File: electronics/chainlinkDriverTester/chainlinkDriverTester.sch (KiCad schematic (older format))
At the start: 147 parts, among them J10 Sensor C, J11 Sensor D, J12 Motor E, J13 Motor F, J14 Sensor E, J15 Sensor F, J22 Power, J26 exp, J27 exp, J28 exp, J29 exp, J3 Motor A, J30 exp, J31 exp, J32 Conn_01x06_Female, J5 Motor B, J6 Motor C, J7 Motor D, J8 Sensor A, J9 Sensor B, U1 AP7361C-33E, U2 TTGO_TDisplay, U3 VN7007ALH, U4 MCP23017_SS, U5 INA219BxD, U6 SN74LV1T34DBV

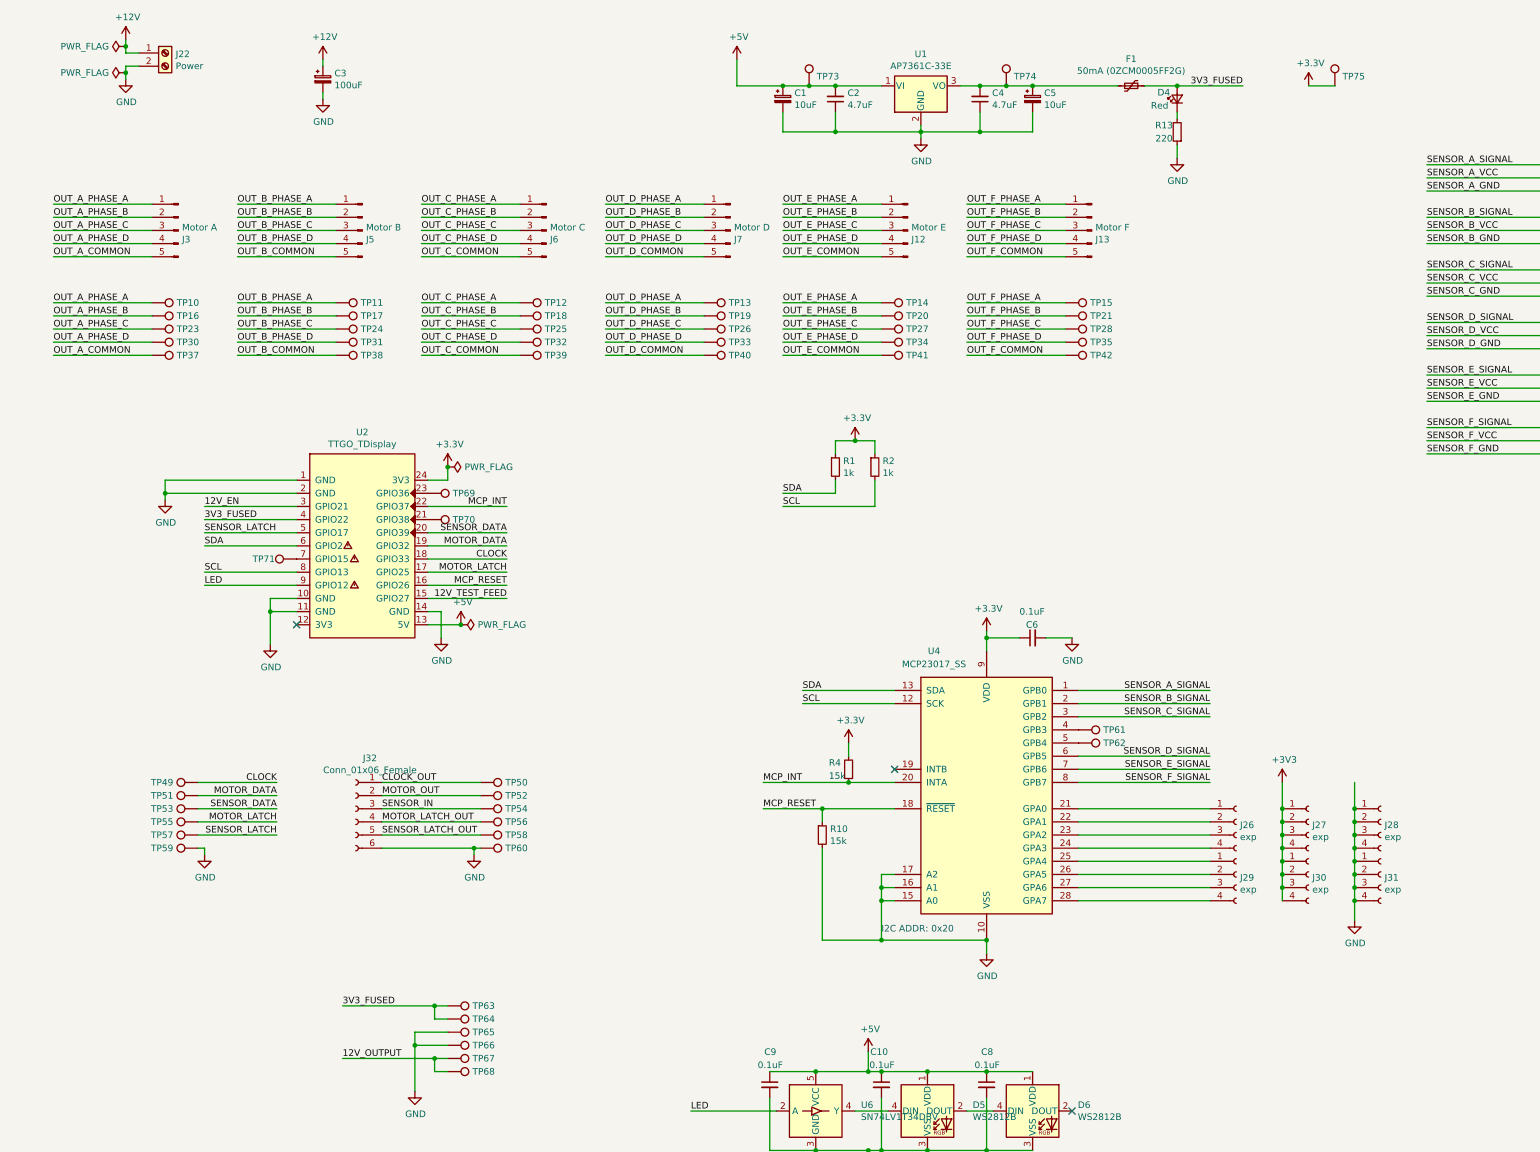
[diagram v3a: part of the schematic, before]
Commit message: PCB updates, add buzzer, add CI
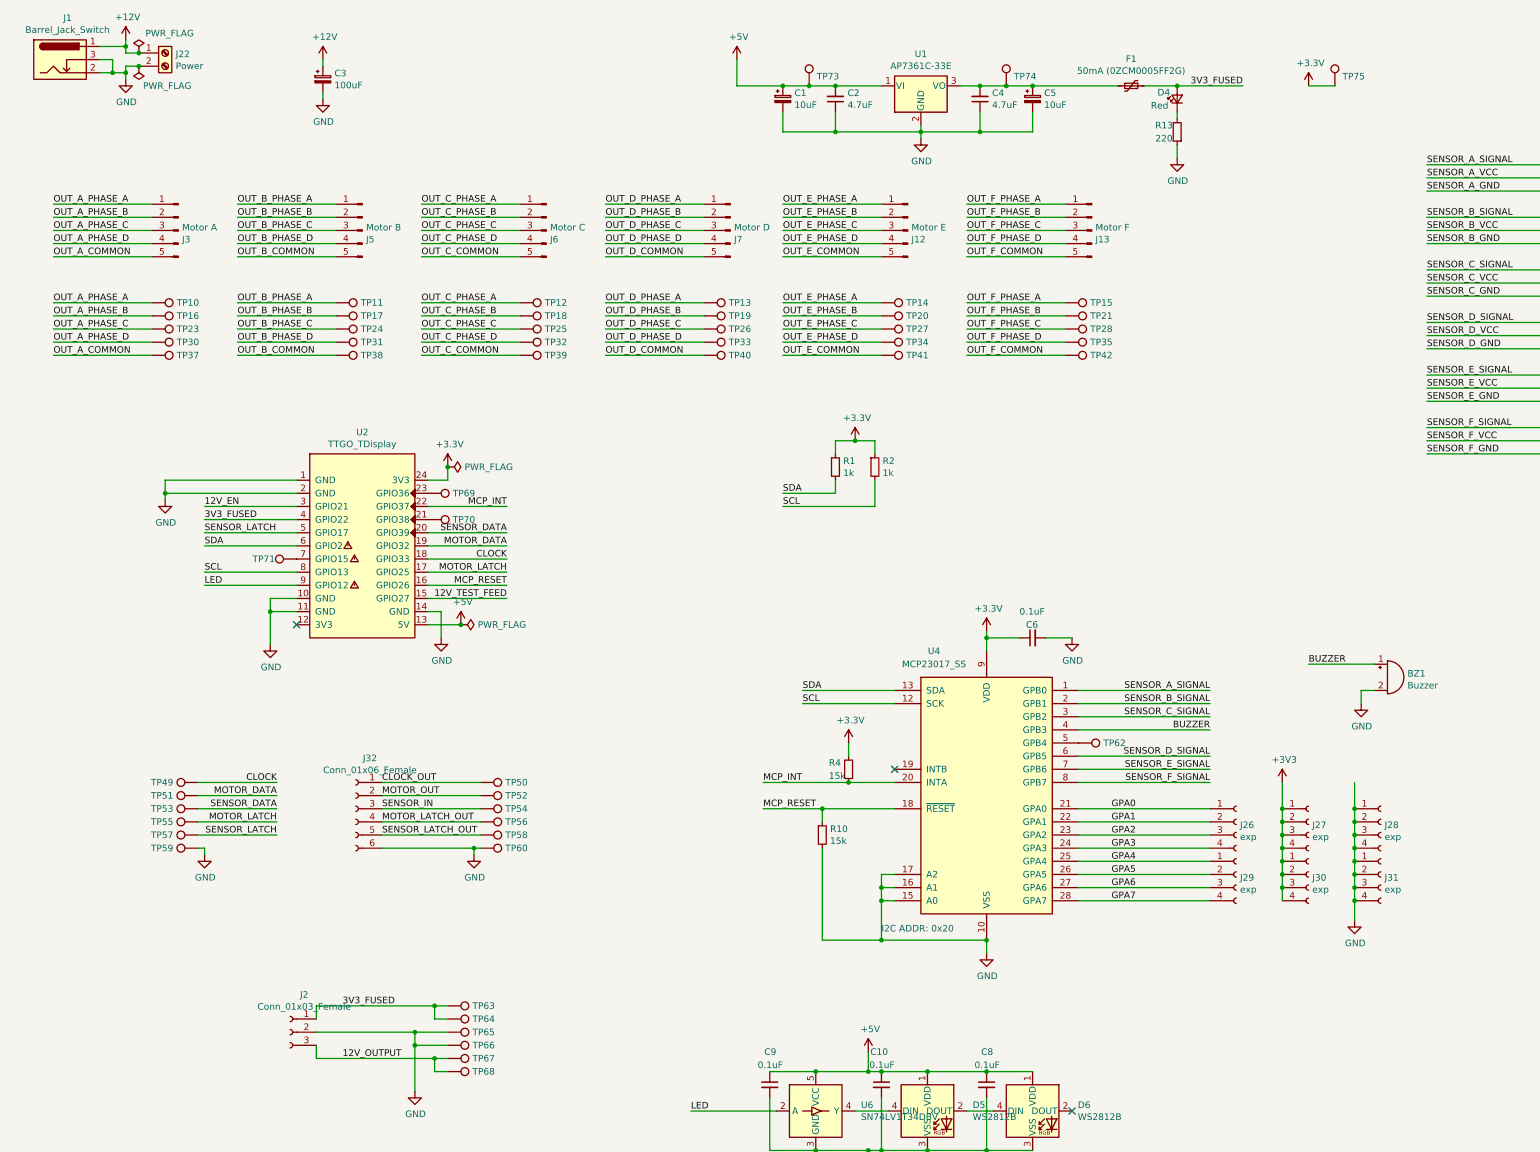
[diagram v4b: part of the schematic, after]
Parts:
- removed TP61: TestPoint, TestPoint:TestPoint_THTPad_D2.0mm_Drill1.0mm, symbol Connector:TestPoint
- added BZ1: Buzzer, Buzzer_Beeper:Buzzer_12x9.5RM7.6, symbol Device:Buzzer
- added J1: Barrel_Jack_Switch, PJ-202A:PJ-202A, symbol Connector:Barrel_Jack_Switch
- added J2: Conn_01x03_Female, Connector_PinSocket_2.54mm:PinSocket_1x03_P2.54mm_Vertical, symbol Connector:Conn_01x03_Female
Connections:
- net +12V: now also J1.1
- net 12V_OUTPUT: now also J2.3 (Pin_3)
- net 3V3_FUSED: now also J2.1 (Pin_1)
- net GND: now also BZ1.2 (+), J1.2, J1.3, J2.2 (Pin_2)
- net GPA0: now reaches J26.1 (Pin_1), U4.21 (GPA0)
- net GPA1: now reaches J26.2 (Pin_2), U4.22 (GPA1)
- net GPA2: now reaches J26.3 (Pin_3), U4.23 (GPA2)
- net GPA3: now reaches J26.4 (Pin_4), U4.24 (GPA3)
- net GPA4: now reaches J29.1 (Pin_1), U4.25 (GPA4)
- net GPA5: now reaches J29.2 (Pin_2), U4.26 (GPA5)
- net GPA6: now reaches J29.3 (Pin_3), U4.27 (GPA6)
- net GPA7: now reaches J29.4 (Pin_4), U4.28 (GPA7)
- net BUZZER: now reaches U4.4 (GPB3)
- net BUZZER: now also BZ1.1 (-)
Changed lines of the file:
@@
 Connection ~ 3650 8500
-Wire Wire Line
-	3650 8500 2950 8500
 Wire Wire Line
 	3750 8300 3500 8300
@@
 $EndComp
 Wire Wire Line
-	1300 1050 1300 1000
-Wire Wire Line
 	1300 950  1400 950
 Wire Wire Line
@@
 L power:PWR_FLAG #FLG0103
 U 1 1 6165DEB7
-P 1300 800
-F 0 "#FLG0103" H 1300 875 50  0001 C CNN
-F 1 "PWR_FLAG" V 1300 927 50  0000 L CNN
-F 2 "" H 1300 800 50  0001 C CNN
-F 3 "~" H 1300 800 50  0001 C CNN
-	1    1300 800
-	0    -1   -1   0
+P 1400 850
+F 0 "#FLG0103" H 1400 925 50  0001 C CNN
+F 1 "PWR_FLAG" H 1450 1000 50  0000 L CNN
+F 2 "" H 1400 850 50  0001 C CNN
+F 3 "~" H 1400 850 50  0001 C CNN
+	1    1400 850
+	1    0    0    -1
 $EndComp
 Connection ~ 1300 800
@@
 Text Label 2950 8100 0    50   ~ 0
 3V3_FUSED
-Wire Wire Line
-	2950 8100 3650 8100
 Connection ~ 3650 8100
 Wire Wire Line
@@
 L power:PWR_FLAG #FLG0106
 U 1 1 6205E226
-P 1300 1000
-F 0 "#FLG0106" H 1300 1075 50  0001 C CNN
-F 1 "PWR_FLAG" V 1300 1127 50  0000 L CNN
-F 2 "" H 1300 1000 50  0001 C CNN
-F 3 "~" H 1300 1000 50  0001 C CNN
-	1    1300 1000
-	0    -1   -1   0
-$EndComp
-Connection ~ 1300 1000
-Wire Wire Line
-	1300 1000 1300 950
+P 1400 950
+F 0 "#FLG0106" H 1400 1025 50  0001 C CNN
+F 1 "PWR_FLAG" H 1000 1100 50  0000 L CNN
+F 2 "" H 1400 950 50  0001 C CNN
+F 3 "~" H 1400 950 50  0001 C CNN
+	1    1400 950
+	-1   0    0    1
+$EndComp
 Wire Wire Line
 	3950 6900 3250 6900
@@
 F 3 "~" H 8750 6100 50  0001 C CNN
 	1    8550 6100
-	0    1    1    0
-$EndComp
-$Comp
-L Connector:TestPoint TP61
-U 1 1 61F7E6FB
-P 8550 6000
-F 0 "TP61" V 8550 6188 50  0000 L CNN
-F 1 "TestPoint" V 8595 6188 50  0001 L CNN
-F 2 "TestPoint:TestPoint_THTPad_D2.0mm_Drill1.0mm" H 8750 6000 50  0001 C CNN
-F 3 "~" H 8750 6000 50  0001 C CNN
-	1    8550 6000
 	0    1    1    0
 $EndComp
@@
 	7850 9200 8200 9200
 NoConn ~ 2600 5200
+Text Label 8800 6600 0    50   ~ 0
+GPA0
+Text Label 8800 6700 0    50   ~ 0
+GPA1
+Text Label 8800 6800 0    50   ~ 0
+GPA2
+Text Label 8800 6900 0    50   ~ 0
+GPA3
+Text Label 8800 7000 0    50   ~ 0
+GPA4
+Text Label 8800 7100 0    50   ~ 0
+GPA5
+Text Label 8800 7200 0    50   ~ 0
+GPA6
+Text Label 8800 7300 0    50   ~ 0
+GPA7
+$Comp
+L Connector:Barrel_Jack_Switch J1
+U 1 1 6074305E
+P 800 900
+F 0 "J1" H 857 1217 50  0000 C CNN
+F 1 "Barrel_Jack_Switch" H 857 1126 50  0000 C CNN
+F 2 "PJ-202A:PJ-202A" H 850 860 50  0001 C CNN
+F 3 "~" H 850 860 50  0001 C CNN
+	1    800  900
+	1    0    0    -1
+$EndComp
+Wire Wire Line
+	1100 800  1300 800
+Wire Wire Line
+	1300 950  1300 1000
+Wire Wire Line
+	1100 1000 1200 1000
+Connection ~ 1300 1000
+Wire Wire Line
+	1300 1000 1300 1050
+Wire Wire Line
+	1100 900  1200 900
+Wire Wire Line
+	1200 900  1200 1000
+Connection ~ 1200 1000
+Wire Wire Line
+	1200 1000 1300 1000
+Connection ~ 1400 850
+Connection ~ 1400 950
+$Comp
+L Connector:Conn_01x03_Female J2
+U 1 1 607CDC54
+P 2550 8300
+F 0 "J2" H 2442 8585 50  0000 C CNN
+F 1 "Conn_01x03_Female" H 2442 8494 50  0000 C CNN
+F 2 "Connector_PinSocket_2.54mm:PinSocket_1x03_P2.54mm_Vertical" H 2550 8300 50  0001 C CNN
+F 3 "~" H 2550 8300 50  0001 C CNN
+	1    2550 8300
+	-1   0    0    -1
+$EndComp
+Wire Wire Line
+	2750 8200 2750 8100
+Wire Wire Line
+	2750 8100 3650 8100
+Wire Wire Line
+	2750 8300 3500 8300
+Connection ~ 3500 8300
+Wire Wire Line
+	2750 8400 2750 8500
+Wire Wire Line
+	2750 8500 3650 8500
+$Comp
+L Device:Buzzer BZ1
+U 1 1 606C3416
+P 10900 5600
+F 0 "BZ1" H 11052 5629 50  0000 L CNN
+F 1 "Buzzer" H 11052 5538 50  0000 L CNN
+F 2 "Buzzer_Beeper:Buzzer_12x9.5RM7.6" V 10875 5700 50  0001 C CNN
+F 3 "~" V 10875 5700 50  0001 C CNN
+F 4 "668-AI-1224-TWT-5V-R-ND" H 10900 5600 50  0001 C CNN "DK#"
+	1    10900 5600
+	1    0    0    -1
+$EndComp
+Wire Wire Line
+	9550 6000 8550 6000
+Text Label 9550 6000 2    50   ~ 0
+BUZZER
+Text Label 10300 5500 0    50   ~ 0
+BUZZER
+Wire Wire Line
+	10300 5500 10800 5500
+$Comp
+L power:GND #PWR06
+U 1 1 60731F39
+P 10700 5800
+F 0 "#PWR06" H 10700 5550 50  0001 C CNN
+F 1 "GND" H 10705 5627 50  0000 C CNN
+F 2 "" H 10700 5800 50  0001 C CNN
+F 3 "" H 10700 5800 50  0001 C CNN
+	1    10700 5800
+	1    0    0    -1
+$EndComp
+Wire Wire Line
+	10700 5800 10700 5700
+Wire Wire Line
+	10700 5700 10800 5700
 $EndSCHEMATC

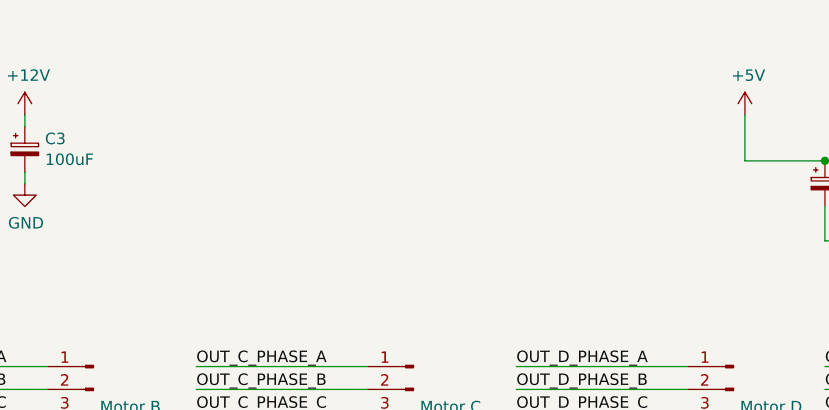
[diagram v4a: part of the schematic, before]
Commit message: Add optional buck module
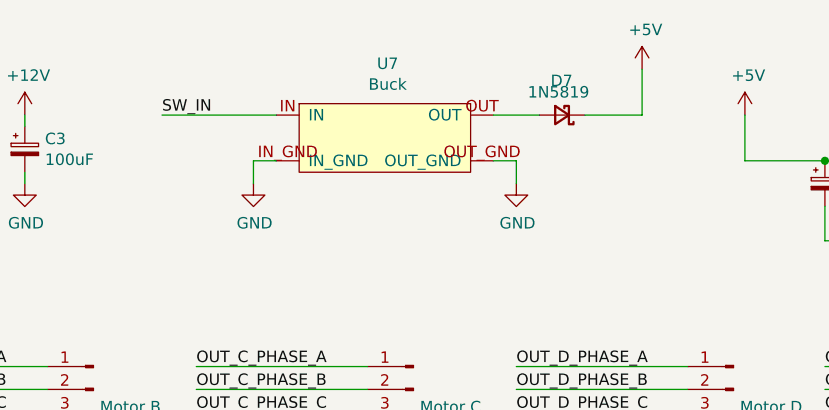
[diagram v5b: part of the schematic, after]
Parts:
- added D7: 1N5819, Diode_SMD:D_SOD-123, symbol Device:D_Schottky_Small
- added U7: Buck, Buck:BuckModule, symbol BuckModule:Buck
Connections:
- net +5V: now also D7.1 (K)
- net GND: now also U7.IN_GND, U7.OUT_GND
- net SW_IN: now also U7.IN
- new net: D7.2 (A), U7.OUT
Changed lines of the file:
@@
 Wire Wire Line
 	10700 5700 10800 5700
+$Comp
+L BuckModule:Buck U7
+U 1 1 60777001
+P 4350 1000
+F 0 "U7" H 4387 1325 50  0000 C CNN
+F 1 "Buck" H 4387 1234 50  0000 C CNN
+F 2 "Buck:BuckModule" H 4350 1000 50  0001 C CNN
+F 3 "" H 4350 1000 50  0001 C CNN
+	1    4350 1000
+	1    0    0    -1
+$EndComp
+Wire Wire Line
+	3900 900  3400 900
+Text Label 3400 900  0    50   ~ 0
+SW_IN
+$Comp
+L power:GND #PWR08
+U 1 1 607A4A3C
+P 3800 1200
+F 0 "#PWR08" H 3800 950 50  0001 C CNN
+F 1 "GND" H 3805 1027 50  0000 C CNN
+F 2 "" H 3800 1200 50  0001 C CNN
+F 3 "" H 3800 1200 50  0001 C CNN
+	1    3800 1200
+	1    0    0    -1
+$EndComp
+Wire Wire Line
+	3800 1200 3800 1100
+Wire Wire Line
+	3800 1100 3900 1100
+$Comp
+L power:GND #PWR09
+U 1 1 607C7992
+P 4950 1200
+F 0 "#PWR09" H 4950 950 50  0001 C CNN
+F 1 "GND" H 4955 1027 50  0000 C CNN
+F 2 "" H 4950 1200 50  0001 C CNN
+F 3 "" H 4950 1200 50  0001 C CNN
+	1    4950 1200
+	1    0    0    -1
+$EndComp
+Wire Wire Line
+	4950 1200 4950 1100
+Wire Wire Line
+	4950 1100 4850 1100
+$Comp
+L power:+5V #PWR07
+U 1 1 607EAE8E
+P 5500 700
+F 0 "#PWR07" H 5500 550 50  0001 C CNN
+F 1 "+5V" H 5515 873 50  0000 C CNN
+F 2 "" H 5500 700 50  0001 C CNN
+F 3 "" H 5500 700 50  0001 C CNN
+	1    5500 700
+	1    0    0    -1
+$EndComp
+Wire Wire Line
+	4850 900  5050 900
+Wire Wire Line
+	5250 900  5500 900
+Wire Wire Line
+	5500 900  5500 700
+$Comp
+L Device:D_Schottky_Small D7
+U 1 1 6086A699
+P 5150 900
+F 0 "D7" H 5200 750 50  0000 R CNN
+F 1 "1N5819" H 5300 800 50  0000 R CNN
+F 2 "Diode_SMD:D_SOD-123" V 5150 900 50  0001 C CNN
+F 3 "~" V 5150 900 50  0001 C CNN
+	1    5150 900
+	-1   0    0    1
+$EndComp
 $EndSCHEMATC
